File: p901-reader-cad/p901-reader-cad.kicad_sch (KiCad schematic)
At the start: 20 parts, among them J1 DE15 (F), J2 5.5mm Barrel (F), U1 MAX232, U2 TPS63060, U3 DOIT ESP32 DevKit v1

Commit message: bump: JLC selections
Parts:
- added C10: 22 μF, Capacitor_SMD:C_0805_2012Metric_Pad1.18x1.45mm_HandSolder, symbol Device:C_Small
- C1, C12, C2, C3, C4: LCSC (none) -> CL21B105KBFNNNE
- C5: LCSC (none) -> CC0805KRX7R9BB104
- C6: LCSC (none) -> CC0805JRNPO9BN100
- C7: value 22 μF -> 22 μF (±10%); footprint Capacitor_SMD:C_0805_2012Metric_Pad1.18x1.45mm_HandSolder -> Capacitor_SMD:C_1206_3216Metric_Pad1.33x1.80mm_HandSolder; LCSC (none) -> CL31A226KAHNNNE
- C9: value 68 μF -> 47 μF; LCSC (none) -> CL31A476MPHNNNE
- DS1, J1, J2, L1, RV1, U3: now left out of the parts list
- R1, R3: LCSC (none) -> 0805W8F1004T5E
- R2: value 111 kΩ -> 110 kΩ; LCSC (none) -> 0805W8F1103T5E
- U1: LCSC (none) -> MAX232DR
- U2: LCSC (none) -> TPS63060DSCR
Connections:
- net +5V: now also C10.1
- net GND: now also C10.2
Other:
- moved on the sheet: C9

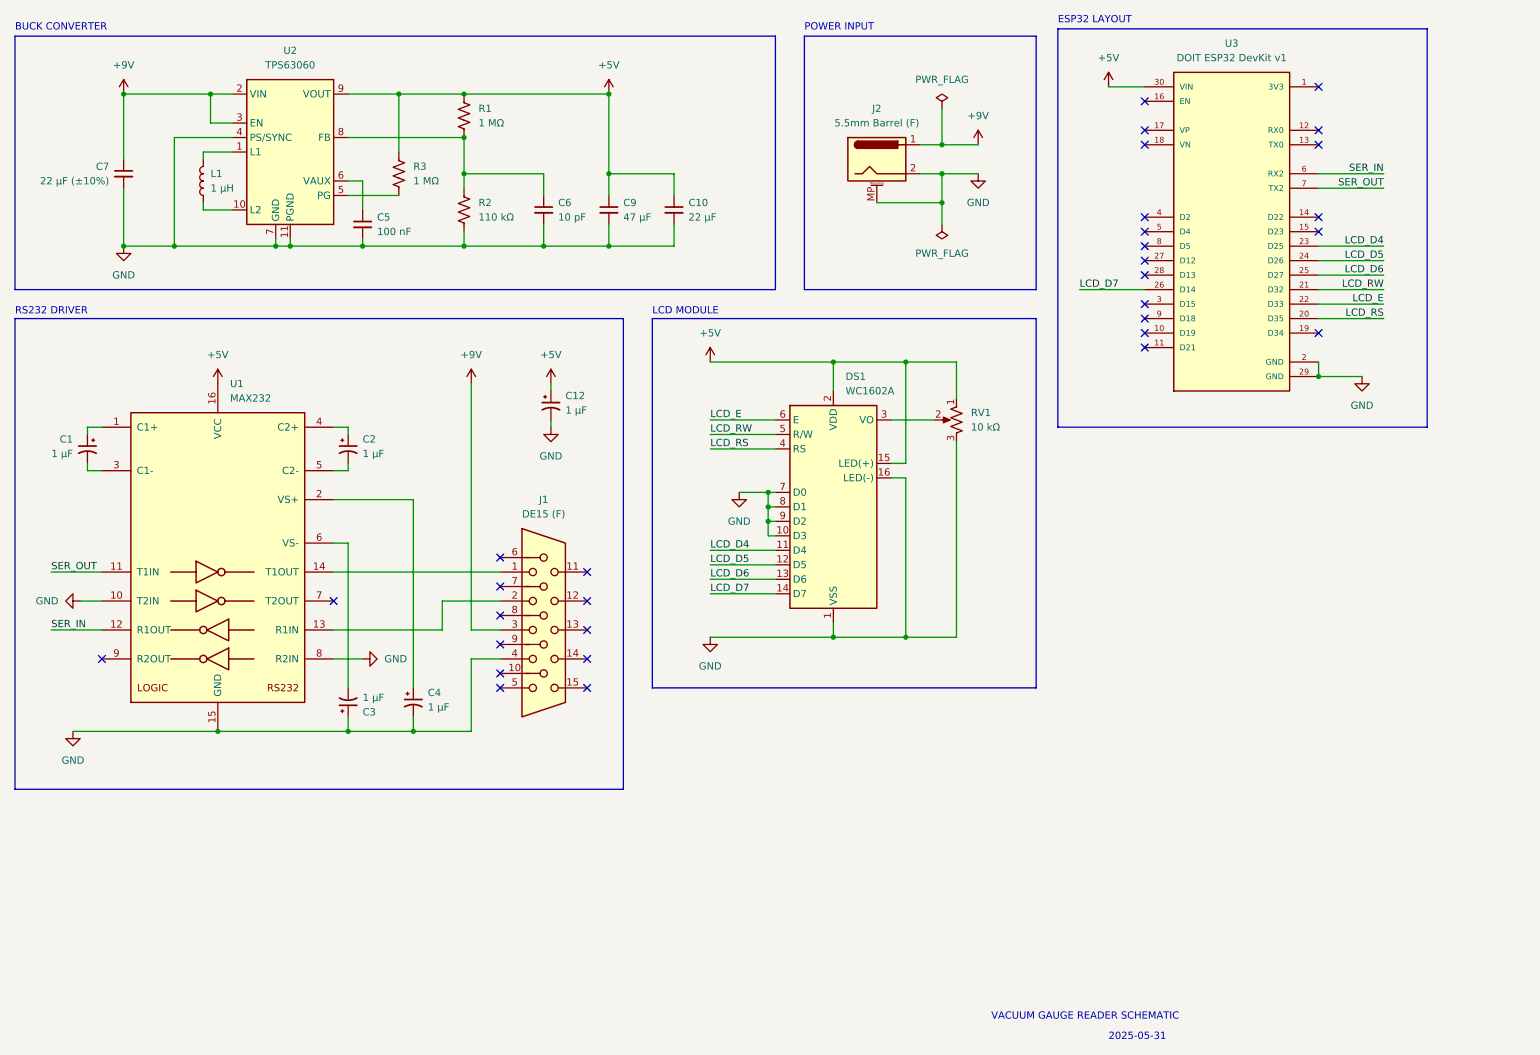
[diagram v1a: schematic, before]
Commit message: update to KiCAD 10.0, reroute against official ESP footprints
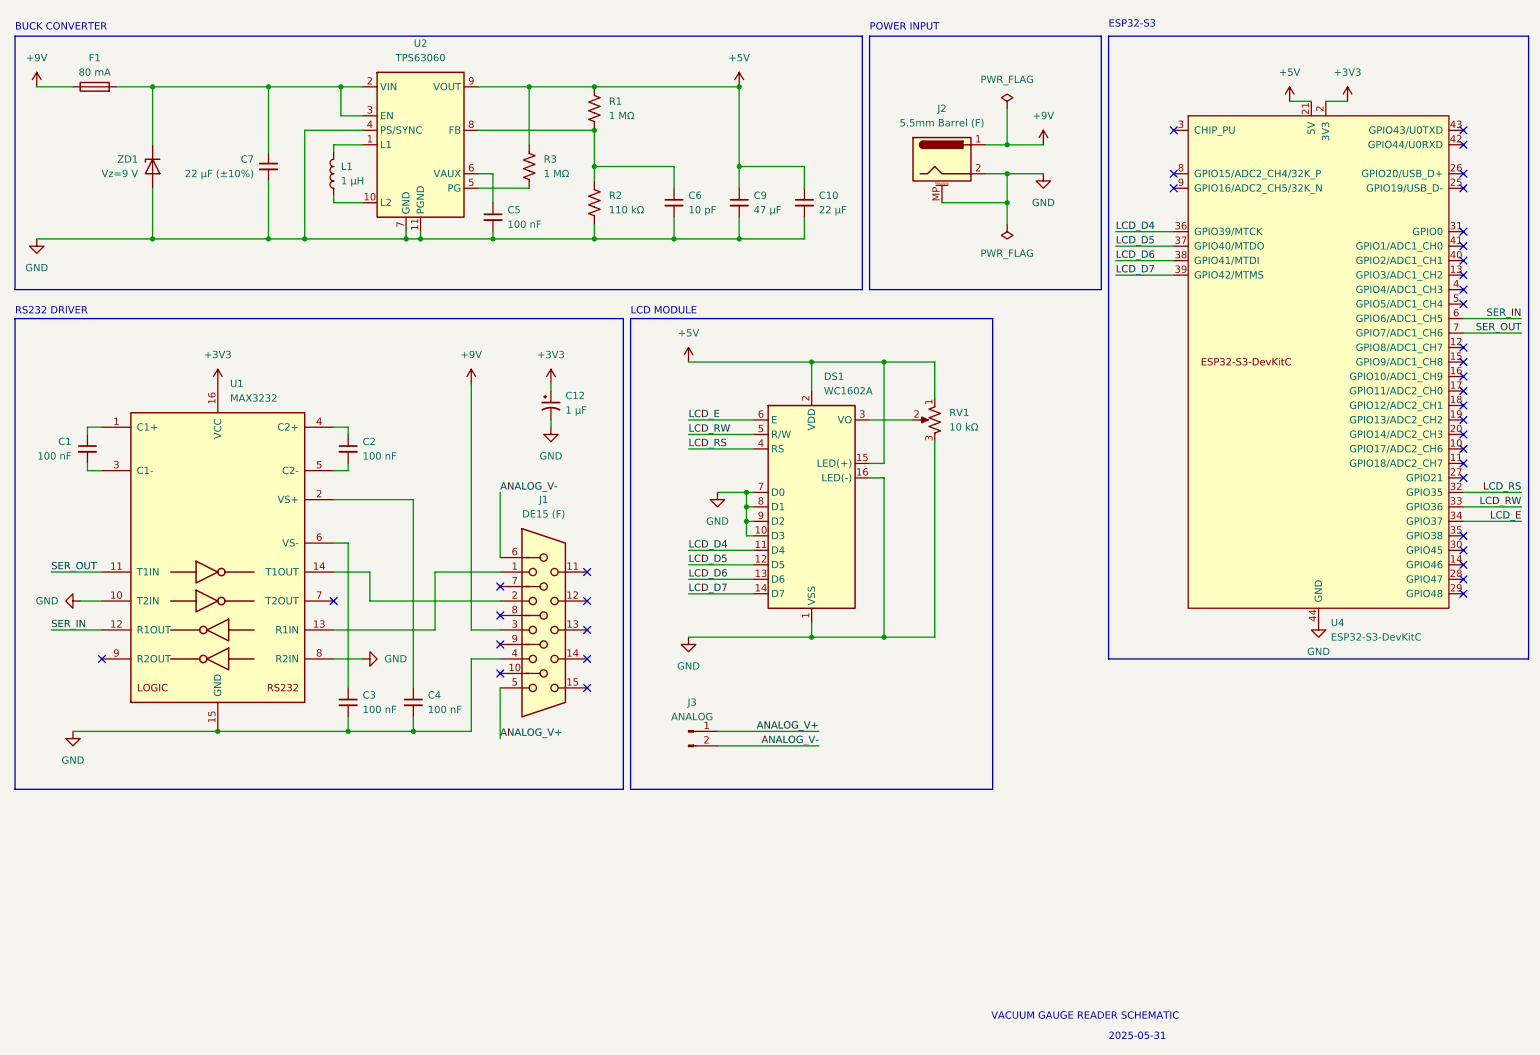
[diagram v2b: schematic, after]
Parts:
- removed C1, C2, C3, C4: 1 μF, Capacitor_SMD:C_0805_2012Metric_Pad1.18x1.45mm_HandSolder, symbol Device:C_Polarized_Small_US
- removed U1: MAX232, TI_MAX232Dx:D16, symbol Interface_UART:MAX232
- removed U3: DOIT ESP32 DevKit v1, ESP32-DEVKIT-V1:MODULE_ESP32_DEVKIT_V1, symbol ESP32-DEVKIT-V1:ESP32-DEVKIT-V1
- added C1, C2, C3, C4: 100 nF, Capacitor_SMD:C_0805_2012Metric_Pad1.18x1.45mm_HandSolder, symbol Device:C_Small
- added F1: 80 mA, Fuse:Fuseholder_TR5_Littelfuse_No560_No460, symbol Device:Fuse
- added J3: ANALOG, Connector_PinSocket_2.54mm:PinSocket_1x02_P2.54mm_Vertical, symbol Connector:Conn_01x02_Pin
- added U1: MAX3232, Package_SO:SOIC-16W_7.5x10.3mm_P1.27mm, symbol Interface_UART:MAX3232
- added U4: ESP32-S3-DevKitC, PCM_Espressif:ESP32-S3-DevKitC, symbol PCM_Espressif:ESP32-S3-DevKitC
- added ZD1: Vz=9 V, Diode_SMD:D_1812_4532Metric, symbol Device:D_Zener
- J1: footprint Connector_Dsub:DSUB-15-HD_Socket_Horizontal_P2.29x2.54mm_EdgePinOffset8.35mm_Housed_MountingHolesOffset10.89mm -> Amphenol_P154XLF:AMPHENOL_10090926-P154XLF
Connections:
- net +5V: now also U4.21 (5V); no longer C12.1
- net +9V: now also F1.1; no longer C7.1, U2.2 (VIN), U2.3 (EN)
- net GND: now also C3.2, C4.2, U1.10 (T2IN), U1.15 (GND), U1.8 (R2IN), U4.22 (GND), U4.23 (GND), U4.24 (GND), U4.44 (GND), ZD1.2 (A)
- net LCD_D4: now also U4.36 (GPIO39/MTCK)
- net LCD_D5: now also U4.37 (GPIO40/MTDO)
- net LCD_D6: now also U4.38 (GPIO41/MTDI)
- net LCD_D7: now also U4.39 (GPIO42/MTMS)
- net LCD_E: now also U4.34 (GPIO37)
- net LCD_RS: now also U4.32 (GPIO35)
- net LCD_RW: now also U4.33 (GPIO36)
- net SER_IN: now also U1.12 (R1OUT), U4.6 (GPIO6/ADC1_CH5)
- net SER_OUT: now also U1.11 (T1IN), U4.7 (GPIO7/ADC1_CH6)
- net at J1.1: now also U1.13 (R1IN)
- net at J1.2: now also U1.14 (T1OUT)
- net ANALOG_V+: now reaches J1.5
- net ANALOG_V+: now also J3.1 (Pin_1)
- net ANALOG_V-: now reaches J1.6
- net ANALOG_V-: now also J3.2 (Pin_2)
- new net: C7.1, F1.2, U2.2 (VIN), U2.3 (EN), ZD1.1 (K)
- new net: C3.1, U1.6 (VS-)
- new net: C1.1, U1.1 (C1+)
- new net: C4.1, U1.2 (VS+)
- new net: C1.2, U1.3 (C1-)
- new net: C2.1, U1.4 (C2+)
- new net: C2.2, U1.5 (C2-)
- new net +3V3: C12.1, U1.16 (VCC), U4.1 (3V3), U4.2 (3V3)
- no-connect marks 31 -> 39
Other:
- note added: "ESP32-S3"
- note removed: "ESP32 LAYOUT"
- moved on the sheet: C10, C5, C6, C7, C9, DS1, J2, L1, R1, R2, R3, RV1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

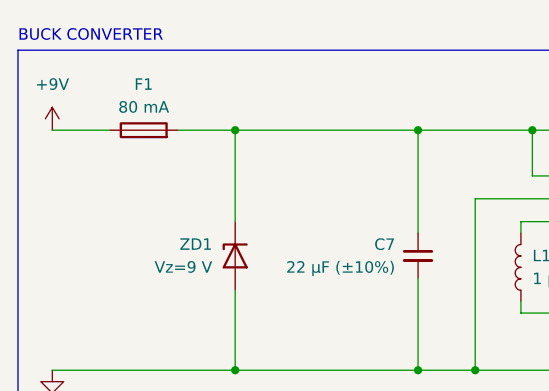
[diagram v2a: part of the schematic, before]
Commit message: redesign power to use USB-C PD
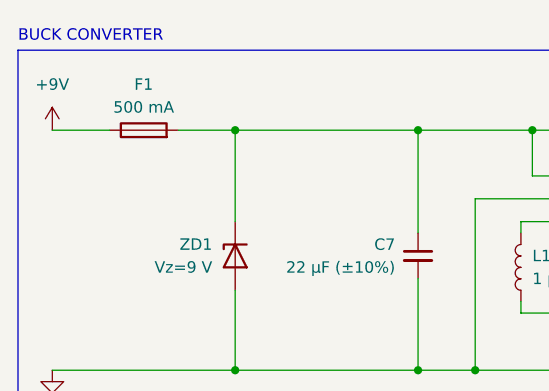
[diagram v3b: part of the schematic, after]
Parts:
- F1: value 80 mA -> 500 mA
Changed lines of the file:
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@@
 			)
 		)
-		(property "Value" "80 mA"
+		(property "Value" "500 mA"
 			(at 29.21 24.13 90)
 			(show_name no)
